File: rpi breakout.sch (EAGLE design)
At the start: 57 parts, among them IC1 PCA9505, J1 RASPBERRYPI-40-PIN-GPIO_PTH, U1 MAX11642EEG, U2 MAX11642EEG, U3 MAX11642EEG

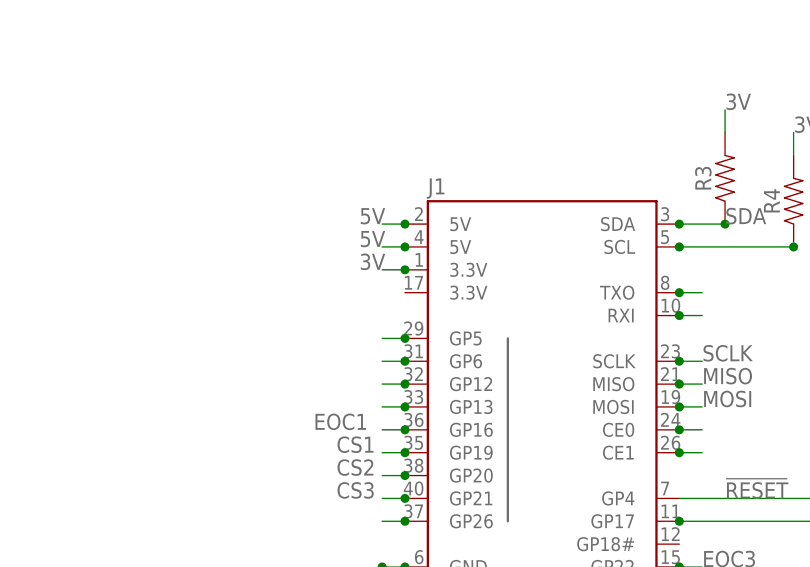
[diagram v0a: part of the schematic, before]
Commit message: updated silkscreen and increased trace sizes
increased sizes of all traces and update routing to clear DRC. Added silkscreen for all connections. Sent to fab
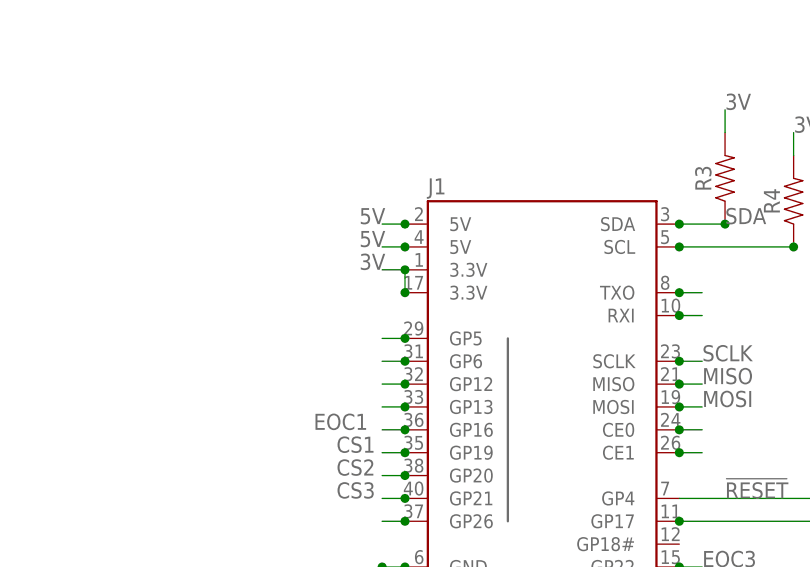
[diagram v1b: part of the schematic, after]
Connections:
- net 3V: now also J1.3.3V@17
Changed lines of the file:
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@@
 <junction x="243.84" y="175.26"/>
 <label x="238.76" y="175.26" size="1.778" layer="95"/>
+<pinref part="J1" gate="G$1" pin="3.3V@17"/>
+<wire x1="243.84" y1="175.26" x2="243.84" y2="172.72" width="0.1524" layer="91"/>
+<junction x="243.84" y="172.72"/>
 </segment>
 <segment>
